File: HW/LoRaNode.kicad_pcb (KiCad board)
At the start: 4 copper layers, 57 x 29 mm, 36 parts, among them J1 UART, J2 I2C, J3 SPI, J4 5V_IN, J5 BAT_IN, J6 SWD, J7 RS485, U1 STM32L071CBTx, U2 E22-900M22S, U3 MAX3483, X1 8MHz, X2 32.768KHz

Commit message: update project and pcb design
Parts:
- added S1: S1, TestPoint:TestPoint_Plated_Hole_D3.0mm, F.Cu at (251.2, 112.9)
- moved S3 10.0 mm to (251.1, 132.9)
- moved ANT1 1.74 mm to (246.6, 118.9)
- renumbered S1 to S4
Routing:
- net GND: track 72.1 -> 177.1 mm
- net /SPI1_MISO: track 39.5 -> 30.7 mm
- net /SPI1_SCK: track 43.8 -> 36.4 mm, vias 0 -> 2
- net Net-(ANT1-Pad1): track 9.30 -> 5.03 mm
- net /SPI1_MOSI: track 35.1 -> 31.6 mm
- net VDD: track 15.9 -> 17.2 mm, vias 7 -> 8
- net /LORA_DIO2: track 42.8 -> 41.6 mm
- net /SPI2_MISO: track 32.5 -> 31.7 mm
- added copper zone on B.Cu, net GND
- added copper zone on F.Cu, net GND
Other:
- board size 57 x 29 mm -> 60 x 30 mm

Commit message: update PCB and Readme
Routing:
- net GND: track 177.1 -> 195.7 mm
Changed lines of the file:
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@@
     (thickness 1.6)
     (drawings 16)
-    (tracks 515)
+    (tracks 526)
     (zones 0)
     (modules 37)
@@
   (page A4)
   (layers
-    (0 F.Cu signal)
-    (1 In1.Cu power)
-    (2 In2.Cu power)
-    (31 B.Cu signal)
-    (32 B.Adhes user)
+    (0 F.Cu signal hide)
+    (1 In1.Cu power hide)
+    (2 In2.Cu power hide)
+    (31 B.Cu signal hide)
+    (32 B.Adhes user hide)
     (33 F.Adhes user hide)
-    (34 B.Paste user)
-    (35 F.Paste user)
-    (36 B.SilkS user)
+    (34 B.Paste user hide)
+    (35 F.Paste user hide)
+    (36 B.SilkS user hide)
     (37 F.SilkS user)
     (38 B.Mask user)
@@
   )
   (setup
-    (last_trace_width 0.1524)
+    (last_trace_width 0.762)
     (user_trace_width 0.1524)
     (user_trace_width 0.2032)
@@
       (effects (font (size 1 1) (thickness 0.15)))
     )
-    (fp_text value S3 (at 0 3) (layer F.Fab)
+    (fp_text value S3 (at 0 3) (layer F.Fab) hide
       (effects (font (size 1 1) (thickness 0.15)))
     )
@@
       (effects (font (size 1 1) (thickness 0.15)))
     )
-    (fp_text value S1 (at 0 3) (layer F.Fab)
+    (fp_text value S1 (at 0 3) (layer F.Fab) hide
       (effects (font (size 1 1) (thickness 0.15)))
     )
@@
       (effects (font (size 1 1) (thickness 0.15)))
     )
-    (fp_text value S4 (at 0 3) (layer F.Fab)
+    (fp_text value S4 (at 0 3) (layer F.Fab) hide
       (effects (font (size 1 1) (thickness 0.15)))
     )
@@
       (effects (font (size 1 1) (thickness 0.15)))
     )
-    (fp_text value S2 (at 0 3) (layer F.Fab)
+    (fp_text value S2 (at 0 3) (layer F.Fab) hide
       (effects (font (size 1 1) (thickness 0.15)))
     )
@@
       (effects (font (size 1 1) (thickness 0.15)))
     )
-    (fp_text value RS485 (at 0.254 -3.81 90) (layer F.Fab)
+    (fp_text value RS485 (at 2.95 2.301 180) (layer F.Fab)
       (effects (font (size 1 1) (thickness 0.15)))
     )
@@
       (effects (font (size 1 1) (thickness 0.15)))
     )
-    (fp_text value BAT_IN (at 0 5.31 90) (layer F.Fab)
-      (effects (font (size 1 1) (thickness 0.15)))
-    )
-    (fp_text user %R (at 0 1.27) (layer F.Fab)
+    (fp_text value BAT_IN (at 1.068 6.895 180) (layer F.Fab)
+      (effects (font (size 1 1) (thickness 0.15)))
+    )
+    (fp_text user %R (at -0.332 5.245) (layer F.Fab)
       (effects (font (size 1 1) (thickness 0.15)))
     )
@@
       (effects (font (size 1 1) (thickness 0.15)))
     )
-    (fp_text value UART (at -2.032 2.032 270) (layer F.Fab)
+    (fp_text value UART (at -2.7835 0.5175 90) (layer F.Fab)
       (effects (font (size 1 1) (thickness 0.15)))
     )
@@
       (effects (font (size 1 1) (thickness 0.15)))
     )
-    (fp_text value N/A (at 0 1.17 90) (layer F.Fab)
+    (fp_text value N/A (at -0.7895 1.7065 90) (layer F.Fab)
       (effects (font (size 1 1) (thickness 0.15)))
     )
@@
       (effects (font (size 1 1) (thickness 0.15)))
     )
-    (fp_text value 18pF (at 0 1.17) (layer F.Fab)
+    (fp_text value 18pF (at 0 1.17) (layer F.Fab) hide
       (effects (font (size 1 1) (thickness 0.15)))
     )
@@
       (effects (font (size 1 1) (thickness 0.15)))
     )
-    (fp_text value 5V_IN (at 0 5.31 90) (layer F.Fab)
+    (fp_text value 5V_IN (at -3 3.416 180) (layer F.Fab)
       (effects (font (size 1 1) (thickness 0.15)))
     )
@@
       (effects (font (size 1 1) (thickness 0.15)))
     )
-    (fp_text value 100nF (at 0 1.17) (layer F.Fab)
+    (fp_text value 100nF (at -0.764 -2.504) (layer F.Fab) hide
       (effects (font (size 1 1) (thickness 0.15)))
     )
@@
       (effects (font (size 1 1) (thickness 0.15)))
     )
-    (fp_text value Ant (at 0 2.05) (layer F.Fab)
+    (fp_text value Ant (at 0 2.05) (layer F.Fab) hide
       (effects (font (size 1 1) (thickness 0.15)))
     )
@@
     (fp_line (start 1.2 -1.2) (end 1.2 1.2) (layer F.SilkS) (width 0.12))
     (fp_line (start -1.2 -1.2) (end 1.2 -1.2) (layer F.SilkS) (width 0.12))
-    (fp_text user %R (at 0 -2) (layer F.Fab)
+    (fp_text user %R (at 0.4 -2.5) (layer F.Fab)
       (effects (font (size 1 1) (thickness 0.15)))
     )
@@
       (effects (font (size 1 1) (thickness 0.15)))
     )
-    (fp_text value 100nF (at 0 1.17) (layer F.Fab)
+    (fp_text value 100nF (at -1.2645 1.3735) (layer F.Fab)
       (effects (font (size 1 1) (thickness 0.15)))
     )
@@
   (segment (start 197.866 133.666) (end 197.9 133.7) (width 0.762) (layer F.Cu) (net 1))
   (segment (start 197.9 133.7) (end 197.9 113.4) (width 0.762) (layer F.Cu) (net 1))
+  (segment (start 243.174 115.714) (end 245.014 115.714) (width 0.762) (layer F.Cu) (net 1))
+  (segment (start 245.014 115.714) (end 246.1 116.8) (width 0.762) (layer F.Cu) (net 1))
+  (segment (start 246.1 116.8) (end 248.55 116.8) (width 0.762) (layer F.Cu) (net 1))
+  (segment (start 248.55 116.8) (end 248.85 117.1) (width 0.762) (layer F.Cu) (net 1))
+  (segment (start 248.85 117.1) (end 248.85 120.95) (width 0.762) (layer F.Cu) (net 1))
+  (segment (start 248.85 120.95) (end 248.55 121.25) (width 0.762) (layer F.Cu) (net 1))
+  (segment (start 248.55 121.25) (end 244.8 121.25) (width 0.762) (layer F.Cu) (net 1))
+  (segment (start 244.8 121.25) (end 244.65 121.1) (width 0.762) (layer F.Cu) (net 1))
+  (segment (start 244.65 121.1) (end 244.65 118.6) (width 0.762) (layer F.Cu) (net 1))
+  (segment (start 244.65 118.6) (end 244.3 118.25) (width 0.762) (layer F.Cu) (net 1))
+  (segment (start 244.3 118.25) (end 243.1 118.25) (width 0.762) (layer F.Cu) (net 1))
   (segment (start 213.233 123.317) (end 213.106 123.317) (width 0.25) (layer F.Cu) (net 2))
   (segment (start 213.067 123.274) (end 213.067 122.721) (width 0.25) (layer F.Cu) (net 2))
@@
       )
     )
+  )
+  (zone (net 1) (net_name GND) (layer In1.Cu) (hatch edge 0.508)
+    (connect_pads (clearance 0.508))
+    (min_thickness 0.254)
+    (fill yes (arc_segments 32) (thermal_gap 0.508) (thermal_bridge_width 0.508))
+    (polygon
+      (pts
+        (xy 249.25 121.75) (xy 241.55 121.8) (xy 241.55 115.7) (xy 249.25 115.7)
+      )
+    )

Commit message: update 3d preview
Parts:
- moved S3 0.77 mm to (251.1, 133.7)
- moved S1 0.10 mm to (251.1, 112.9)
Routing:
- net GND: track 195.7 -> 211.5 mm
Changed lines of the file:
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@@
   (general
     (thickness 1.6)
-    (drawings 16)
-    (tracks 526)
+    (drawings 7)
+    (tracks 527)
     (zones 0)
     (modules 37)
@@
   (page A4)
   (layers
-    (0 F.Cu signal hide)
-    (1 In1.Cu power hide)
-    (2 In2.Cu power hide)
-    (31 B.Cu signal hide)
-    (32 B.Adhes user hide)
-    (33 F.Adhes user hide)
-    (34 B.Paste user hide)
-    (35 F.Paste user hide)
-    (36 B.SilkS user hide)
+    (0 F.Cu signal)
+    (1 In1.Cu power)
+    (2 In2.Cu power)
+    (31 B.Cu signal)
+    (32 B.Adhes user)
+    (33 F.Adhes user)
+    (34 B.Paste user)
+    (35 F.Paste user)
+    (36 B.SilkS user)
     (37 F.SilkS user)
     (38 B.Mask user)
@@
   )
   (module TestPoint:TestPoint_Plated_Hole_D3.0mm (layer F.Cu)
-    (at 251.1 132.9)
+    (at 251.1 133.6675)
     (descr "Plated Hole as test Point, diameter 3.0mm")
     (tags "test point plated hole")
@@
   )
   (module TestPoint:TestPoint_Plated_Hole_D3.0mm (layer F.Cu)
-    (at 251.2 112.9)
+    (at 251.1 112.9)
     (descr "Plated Hole as test Point, diameter 3.0mm")
     (tags "test point plated hole")
@@
       (effects (font (size 1 1) (thickness 0.15)))
     )
-    (pad 1 thru_hole circle (at 0 0) (size 4 4) (drill 3) (layers *.Cu *.Mask)
+    (pad 1 thru_hole circle (at 0 -0.003) (size 4 4) (drill 3) (layers *.Cu *.Mask)
       (net 1 GND))
   )
@@
       (rotate (xyz 0 0 0))
     )
+    (model ${KISYS3DMOD}/Package_SO.3dshapes/HTSOP-8-1EP_3.9x4.9mm_Pitch1.27mm.step
+      (at (xyz 0 0 0))
+      (scale (xyz 1 1 1))
+      (rotate (xyz 0 0 0))
+    )
   )
   (module Resistor_SMD:R_0402_1005Metric (layer F.Cu)
@@
     (arrow2b (pts (xy 188.5 137.7) (xy 187.913579 136.573496)))
   )
-  (target plus (at 197.866 133.6675) (size 5) (width 0.05) (layer Edge.Cuts))
-  (target plus (at 197.866 133.6675) (size 5) (width 0.05) (layer Edge.Cuts))
-  (target plus (at 197.8025 133.6675) (size 5) (width 0.05) (layer Edge.Cuts))
   (gr_line (start 194.5 137.7) (end 194.5 107.7) (layer Edge.Cuts) (width 0.5))
   (gr_line (start 254.5 107.7) (end 254.5 137.7) (layer Edge.Cuts) (width 0.5))
   (gr_line (start 194.5 107.7) (end 254.5 107.7) (layer Edge.Cuts) (width 0.5))
-  (target plus (at 197.8025 133.6675) (size 5) (width 0.05) (layer Edge.Cuts))
-  (target plus (at 197.8025 133.6675) (size 5) (width 0.05) (layer Edge.Cuts))
   (gr_line (start 194.5 137.7) (end 254.5 137.7) (layer Edge.Cuts) (width 0.5))
-  (target plus (at 197.8025 133.6675) (size 5) (width 0.05) (layer Edge.Cuts))
-  (target plus (at 197.8025 133.6675) (size 5) (width 0.05) (layer Edge.Cuts))
-  (target plus (at 197.8025 133.6675) (size 5) (width 0.05) (layer Edge.Cuts))
-  (target plus (at 197.8025 133.6675) (size 5) (width 0.05) (layer Edge.Cuts))
   (target plus (at 197.8025 133.6675) (size 5) (width 0.05) (layer Edge.Cuts))
   (segment (start 213.995 116.205) (end 215.011 116.205) (width 0.25) (layer F.Cu) (net 1))
@@
   (segment (start 219.5195 133.6675) (end 220.98 133.6675) (width 0.254) (layer F.Cu) (net 1))
   (segment (start 197.8025 113.0025) (end 197.5 112.7) (width 0.508) (layer F.Cu) (net 1))
-  (segment (start 197.866 112.903) (end 197.866 109.334) (width 0.508) (layer F.Cu) (net 1))
-  (segment (start 197.866 109.334) (end 198.5 108.7) (width 0.508) (layer F.Cu) (net 1))
   (segment (start 198.5 108.7) (end 247.5 108.7) (width 0.508) (layer F.Cu) (net 1))
   (segment (start 243.174 115.714) (end 241.686 115.714) (width 0.762) (layer F.Cu) (net 1))
@@
   (segment (start 239.4 113.6) (end 239.4 112.4) (width 0.762) (layer F.Cu) (net 1))
   (segment (start 239.4 112.4) (end 239.3 112.3) (width 0.762) (layer F.Cu) (net 1))
-  (segment (start 197.866 112.903) (end 197.866 133.666) (width 0.762) (layer F.Cu) (net 1))
-  (segment (start 197.866 133.666) (end 197.9 133.7) (width 0.762) (layer F.Cu) (net 1))
-  (segment (start 197.9 133.7) (end 197.9 113.4) (width 0.762) (layer F.Cu) (net 1))
   (segment (start 243.174 115.714) (end 245.014 115.714) (width 0.762) (layer F.Cu) (net 1))
   (segment (start 245.014 115.714) (end 246.1 116.8) (width 0.762) (layer F.Cu) (net 1))
@@
   (segment (start 244.65 118.6) (end 244.3 118.25) (width 0.762) (layer F.Cu) (net 1))
   (segment (start 244.3 118.25) (end 243.1 118.25) (width 0.762) (layer F.Cu) (net 1))
+  (segment (start 197.866 108.984) (end 198.2 108.65) (width 0.762) (layer F.Cu) (net 1))
+  (segment (start 197.866 112.903) (end 197.866 108.984) (width 0.762) (layer F.Cu) (net 1))
+  (segment (start 198.2 108.65) (end 198.5 108.7) (width 0.508) (layer F.Cu) (net 1))
+  (segment (start 198.2 108.65) (end 250.05 108.65) (width 0.762) (layer F.Cu) (net 1))
+  (segment (start 250.05 108.65) (end 251.25 109.85) (width 0.762) (layer F.Cu) (net 1))
+  (segment (start 251.25 109.85) (end 251.25 112.95) (width 0.762) (layer F.Cu) (net 1))
   (segment (start 213.233 123.317) (end 213.106 123.317) (width 0.25) (layer F.Cu) (net 2))
   (segment (start 213.067 123.274) (end 213.067 122.721) (width 0.25) (layer F.Cu) (net 2))

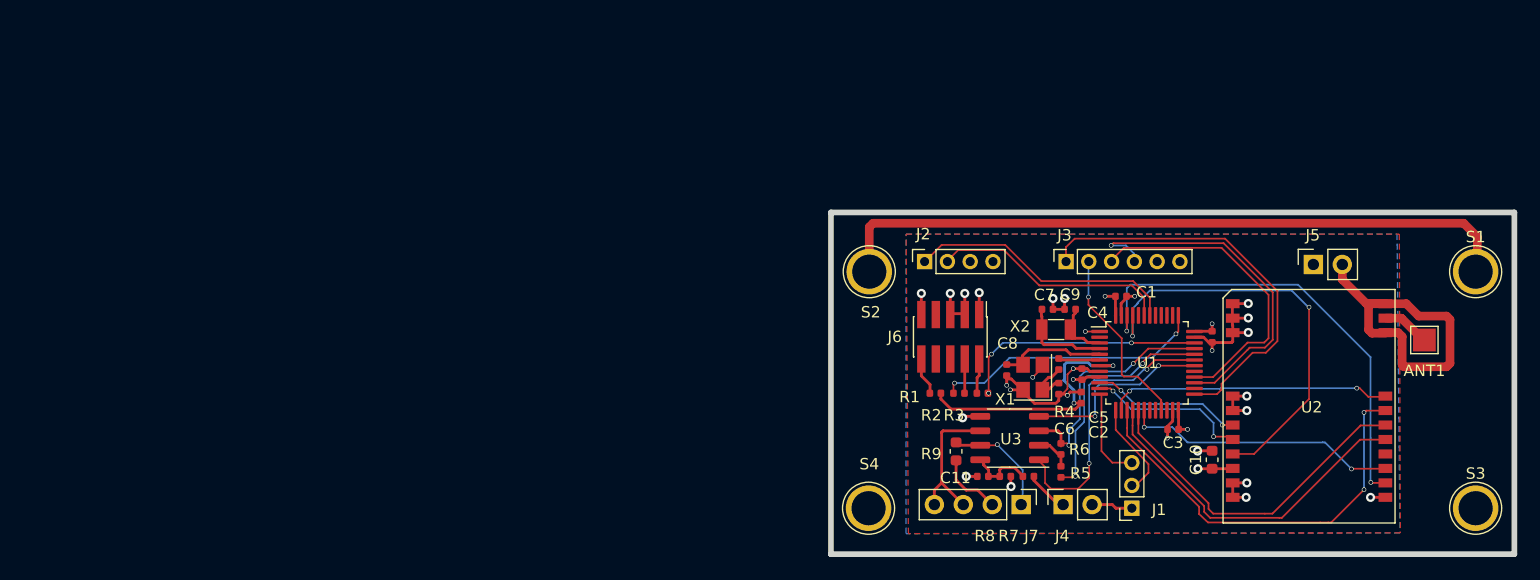
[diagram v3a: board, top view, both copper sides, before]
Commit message: add lost decouple capacitor
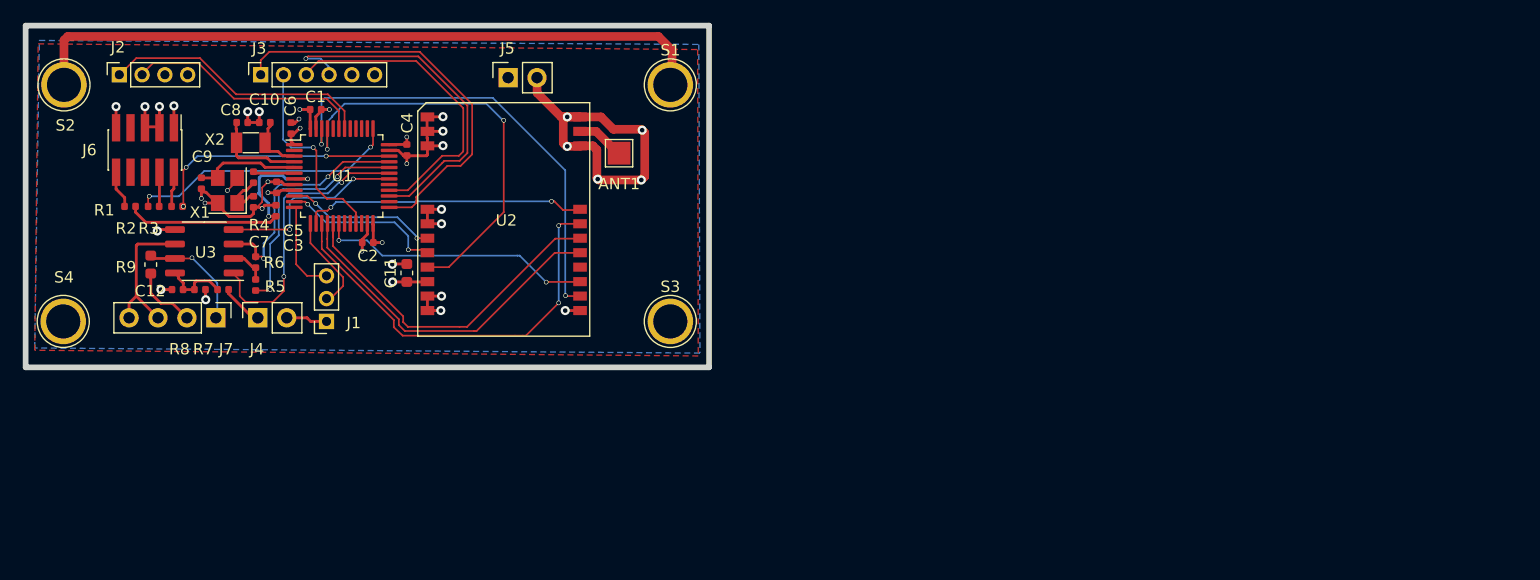
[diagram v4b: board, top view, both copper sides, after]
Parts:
- added C6: 100nF, Capacitor_SMD:C_0402_1005Metric, F.Cu at (147.1, 100.3)
- moved C10 72.6 mm to (144.8, 99.8)
- moved C11 72.6 mm to (157.3, 113.0)
- moved C4 72.6 mm to (157.3, 102.2)
- moved C9 72.6 mm to (139.2, 105.1)
- moved J1 72.6 mm to (150.2, 117.3)
- moved J3 72.6 mm to (144.4, 95.6)
- moved J6 72.6 mm to (134.3, 102.2)
- moved R2 72.6 mm to (135.0, 107.2)
- moved R7 72.6 mm to (141.1, 114.5)
- moved S2 72.6 mm to (127.2, 96.5)
- moved X1 72.6 mm to (141.5, 105.8)
- moved X2 72.6 mm to (143.6, 101.6)
- moved S4 72.6 mm to (127.1, 117.3)
- moved ANT1 72.6 mm to (175.9, 102.5)
- moved C1 72.6 mm to (149.3, 98.7)
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- renumbered C9 to C10, C10 to C11, C11 to C12, C3 to C2, C2 to C3, C6 to C7, C7 to C8, C8 to C9
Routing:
- net VDD: track 17.2 -> 20.1 mm
- net GND: track 211.5 -> 213.2 mm, vias 24 -> 30
- net /SPI2_SCK: track 17.2 -> 18.4 mm
